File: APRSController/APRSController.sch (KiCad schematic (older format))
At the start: 30 parts, among them J1 Conn_01x06, J10 Conn_01x02, J2 Conn_01x02, J3 Conn_01x02, J4 Conn_01x02, J5 Conn_01x02, J6 Conn_01x02, J7 Conn_01x02, J8 Conn_01x02, J9 Conn_01x02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

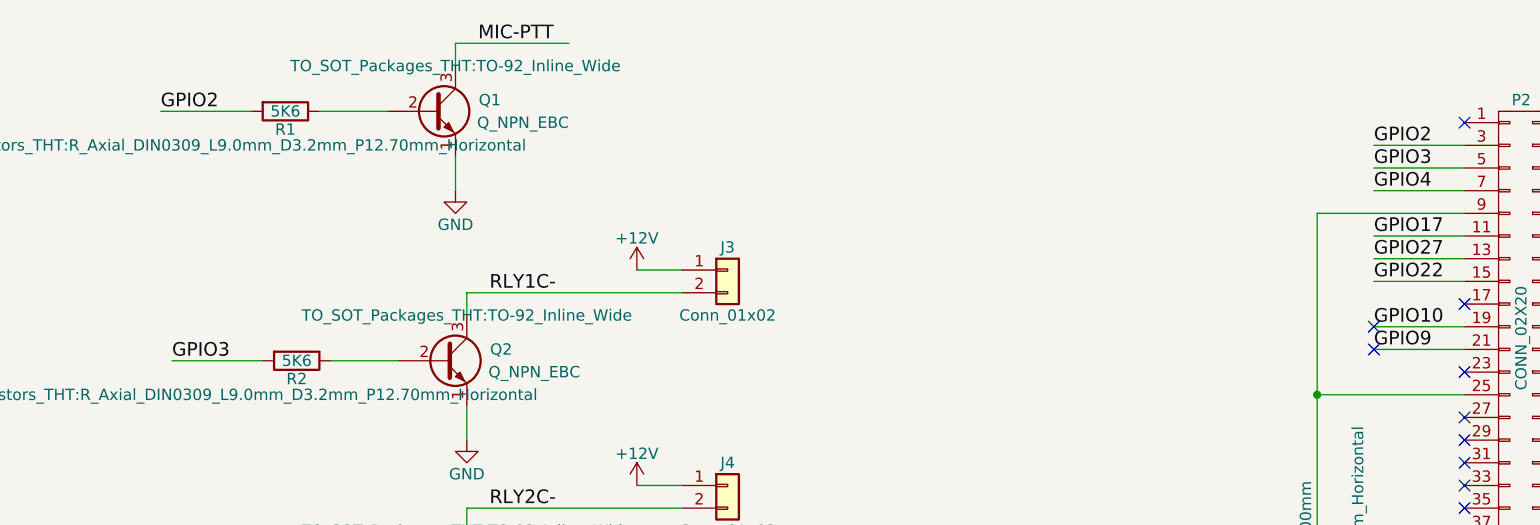
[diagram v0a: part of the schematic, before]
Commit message: Changed controller circuit so as to avoid the I2C lines on the Pi. PTT is now GPIO10.  First output is now GPIO9.
Added two-tone calibration audio to manual test package.
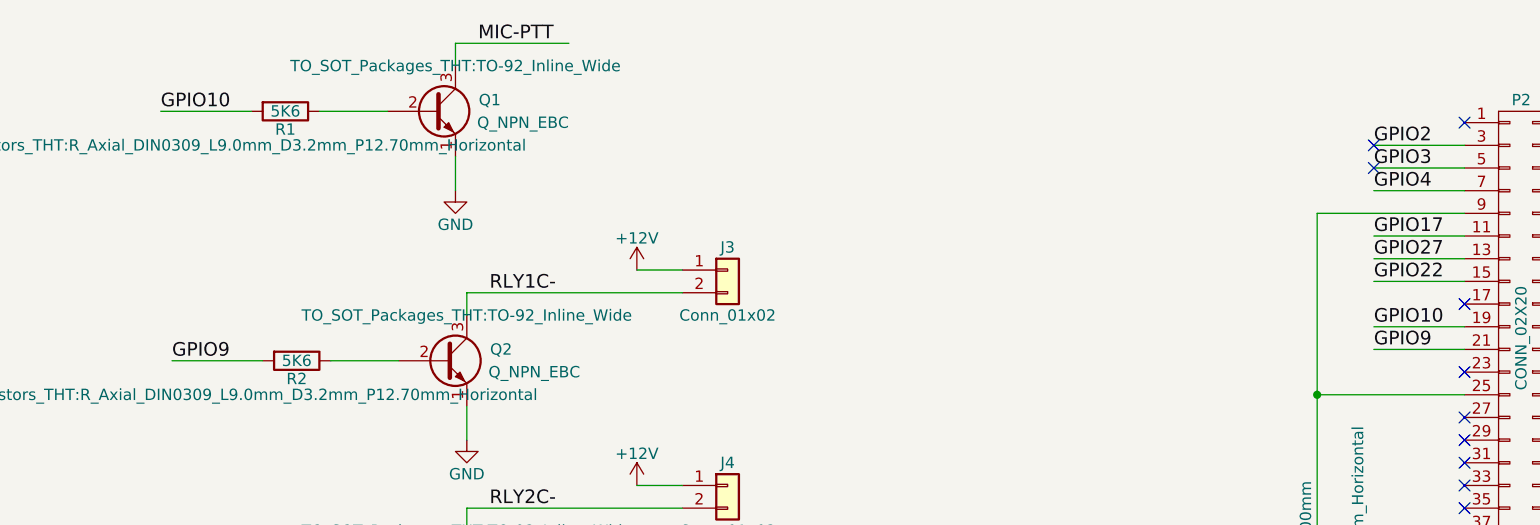
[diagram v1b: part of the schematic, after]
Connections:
- net GPIO10: now also R1.2
- net GPIO2: no longer R1.2
- net GPIO3: no longer R2.2
- net GPIO9: now also R2.2
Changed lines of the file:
@@
 	3300 1000 3800 1000
 Text Label 2000 1300 0    60   ~ 0
-GPIO2
+GPIO10
 Wire Wire Line
 	2000 1300 2400 1300
@@
 	3350 2100 4300 2100
 Text Label 2050 2400 0    60   ~ 0
-GPIO3
+GPIO9
 Wire Wire Line
 	2050 2400 2450 2400
@@
 NoConn ~ 6300 5650
 NoConn ~ 6300 5750
-NoConn ~ 7350 2350
-NoConn ~ 7350 2250
+NoConn ~ 7350 1450
+NoConn ~ 7350 1550
 $EndSCHEMATC
